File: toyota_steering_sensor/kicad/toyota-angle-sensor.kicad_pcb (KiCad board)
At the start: 2 copper layers, 32 parts, among them IC1 ATMEGA328PB-AU, IC2 LS7366R, IC3 AS5047P, J1 AVR-ISP-6, J2 RJ45, U1 NCP1117-5.0_SOT223, U2 MCP2515-xSO, U3 TJA1051T-3, Y1 16MHz, Y2 40MHz, Y3 8MHz

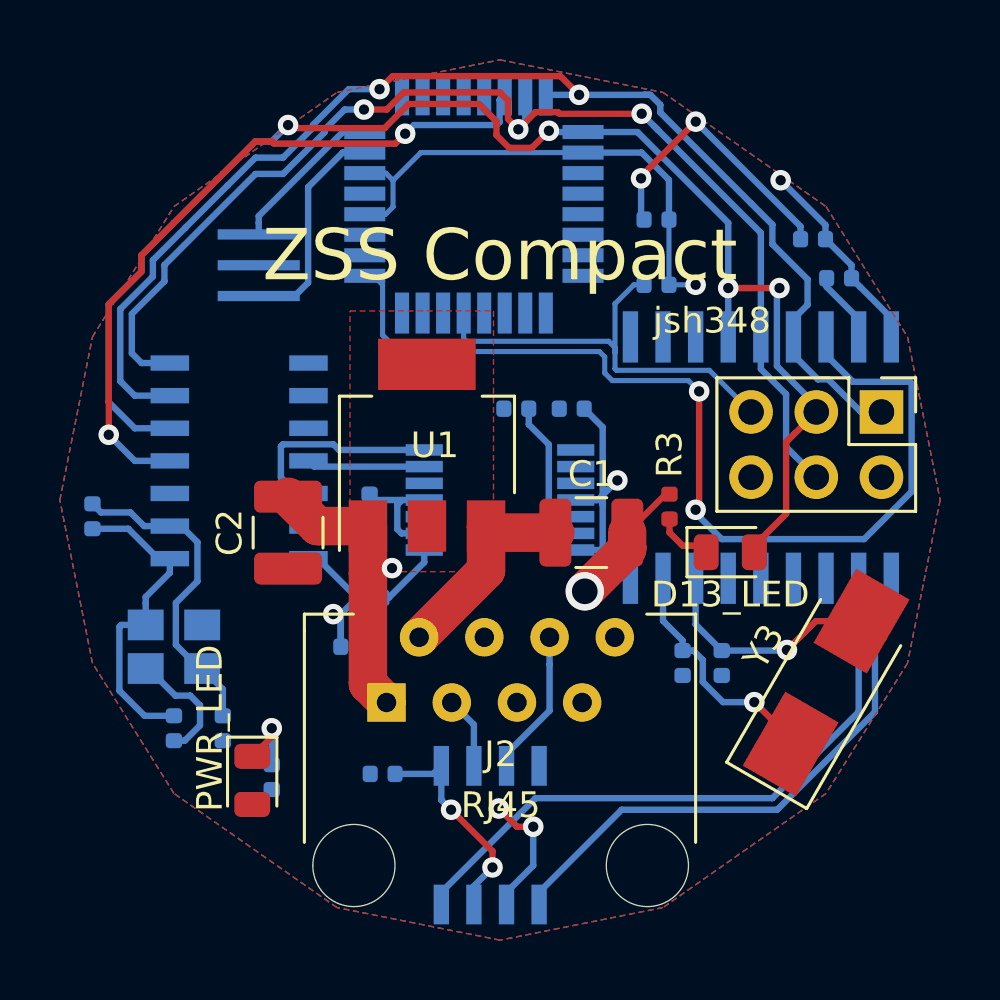
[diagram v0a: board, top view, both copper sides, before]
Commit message: moved atmega chip slightly to pass design rule check
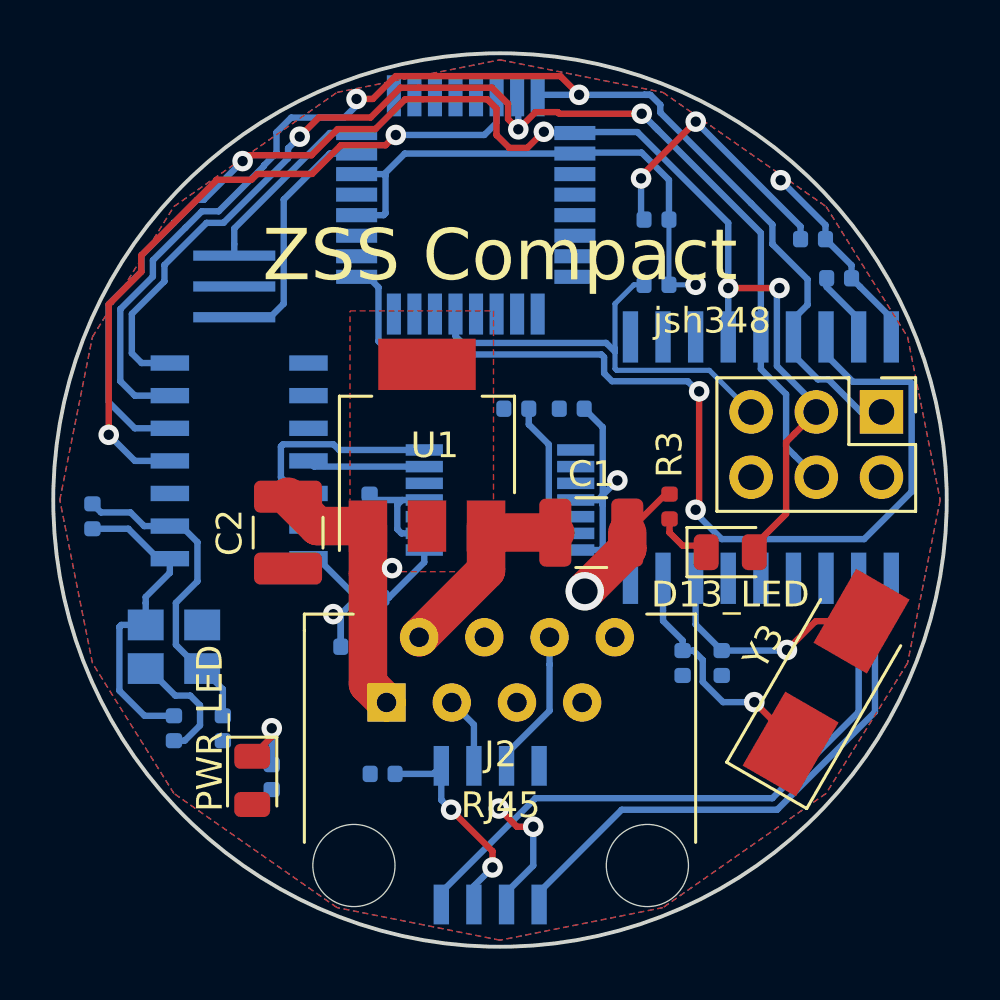
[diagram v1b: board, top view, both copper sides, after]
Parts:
- moved Y1 1.26 mm to (116.6, 118.7)
- moved IC1 0.32 mm to (125.7, 115.5)
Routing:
- net Net-(IC1-Pad7): track 8.62 -> 9.78 mm
- net Net-(IC1-Pad8): track 6.20 -> 7.36 mm
- net /D12,MISO: track 48.8 -> 49.7 mm
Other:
- board outline added: 34.8 x 34.8 mm

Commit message: modify text
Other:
- board text added: "Compact ZSS"
- board text removed: "ZSS Compact"
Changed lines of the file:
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@@
     (effects (font (size 1 1) (thickness 0.15)))
   )
-  (gr_text "ZSS Compact" (at 127 117.475) (layer F.SilkS)
+  (gr_text "Compact ZSS" (at 127 117.475) (layer F.SilkS)
     (effects (font (size 2 2) (thickness 0.15)))
   )

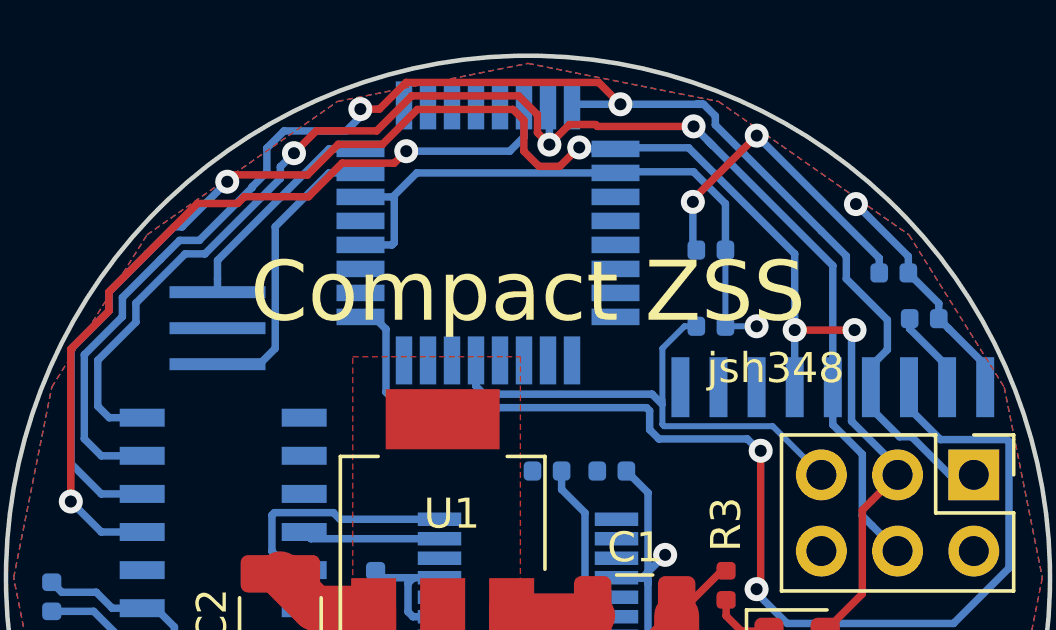
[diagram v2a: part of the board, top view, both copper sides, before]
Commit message: change texts on board
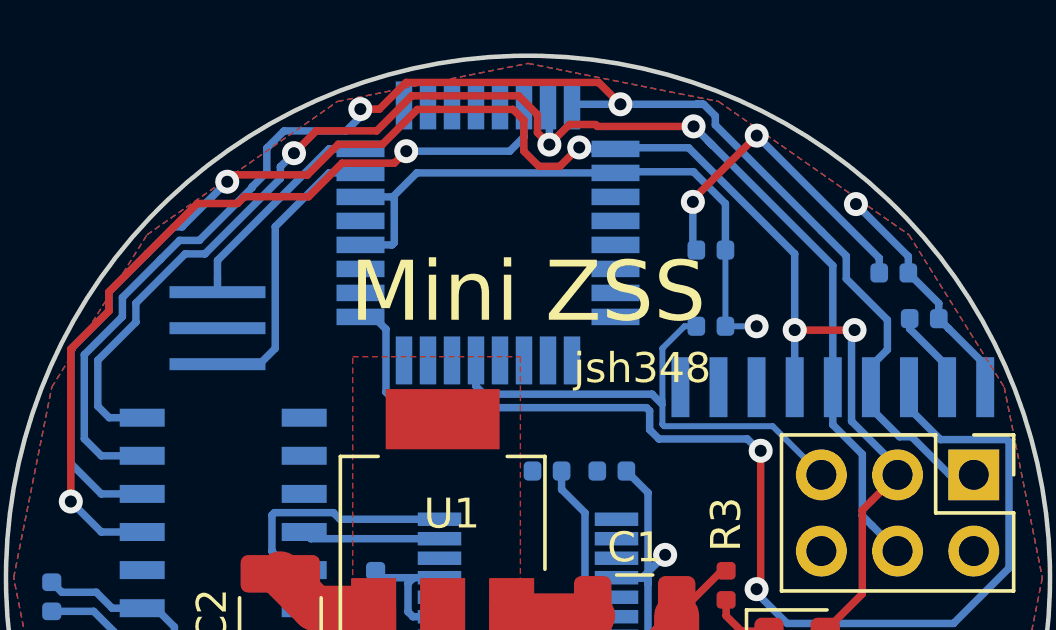
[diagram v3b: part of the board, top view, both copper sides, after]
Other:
- board text added: "Mini ZSS"
- board text removed: "Compact ZSS"
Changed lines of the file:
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@@
     (effects (font (size 1 1) (thickness 0.15)) (justify mirror))
   )
-  (gr_text jsh348 (at 135.255 120.015) (layer F.SilkS)
+  (gr_text jsh348 (at 130.81 120.015) (layer F.SilkS)
     (effects (font (size 1 1) (thickness 0.15)))
   )
-  (gr_text "Compact ZSS" (at 127 117.475) (layer F.SilkS)
+  (gr_text "Mini ZSS" (at 127 117.475) (layer F.SilkS)
     (effects (font (size 2 2) (thickness 0.15)))
   )

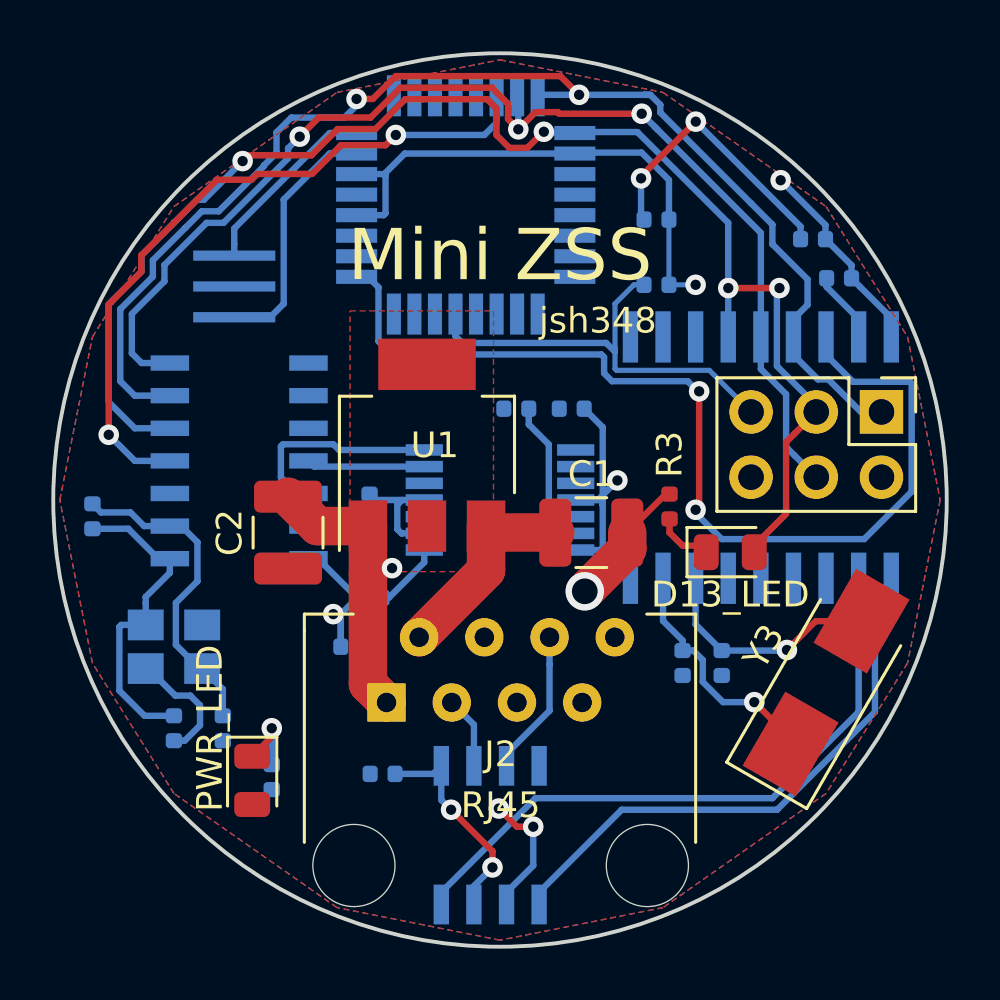
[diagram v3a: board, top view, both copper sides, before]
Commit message: change resistor and capacitor from 0402 to 0603
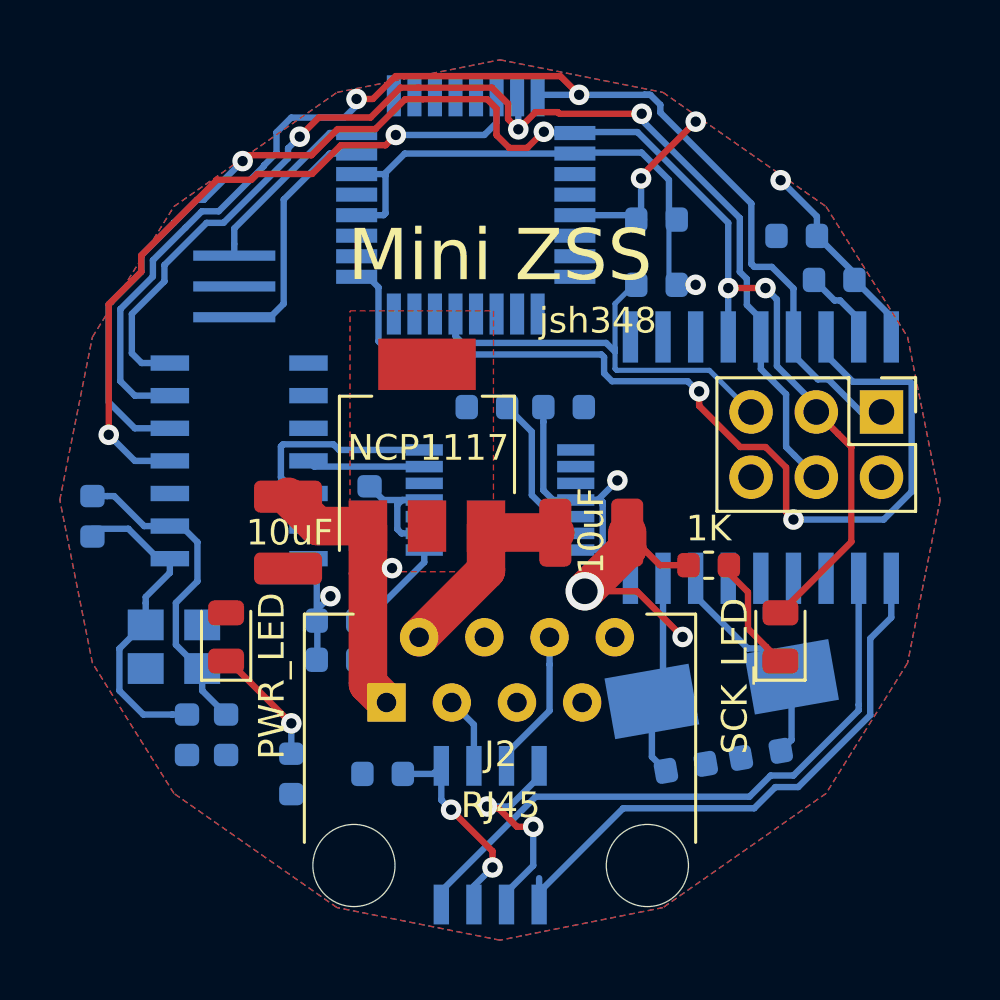
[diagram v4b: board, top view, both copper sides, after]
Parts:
- C10, C11, C12, C3, C4, C5, C6, C7, C8, C9: footprint Capacitor_SMD:C_0402_1005Metric -> Capacitor_SMD:C_0603_1608Metric
- D2: value D13_LED -> SCK_LED
- R1, R2, R3, R4, R5, R6, R7: footprint Resistor_SMD:R_0402_1005Metric -> Resistor_SMD:R_0603_1608Metric
- Y3: moved to B.Cu
- moved D1 5.68 mm to (116.3, 132.3), turned to 90 degrees
- moved Y3 4.07 mm to (135.6, 134.4), turned to 10 degrees
- moved C6 4.07 mm to (134.2, 137.4), turned to 10 degrees
- moved C5 3.87 mm to (137.2, 136.9), turned to 190 degrees
- moved D2 3.84 mm to (137.9, 132.3), turned to 90 degrees
- moved R3 2.75 mm to (135.1, 129.5), turned to 180 degrees
- moved R6 1.55 mm to (120.7, 131.7)
- moved C7 1.14 mm to (126.5, 123.4)
- moved C9 0.81 mm to (120.7, 133.2)
- moved R2 0.77 mm to (118.9, 137.7)
- moved C10 0.65 mm to (138.6, 116.7)
- moved C4 0.57 mm to (114.8, 136.1)
- moved C12 0.32 mm to (129.5, 123.4), turned to 0 degrees
- moved C3 0.28 mm to (116.3, 136.1)
- moved R5 0.20 mm to (140.0, 118.4)
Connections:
- IC1 pad 10: (no net) -> Net-(IC1-Pad10)
- IC1 pad 11: (no net) -> Net-(IC1-Pad11)
- IC1 pad 12: (no net) -> Net-(IC1-Pad12)
- IC1 pad 13: (no net) -> Net-(IC1-Pad13)
- IC1 pad 19: (no net) -> Net-(IC1-Pad19)
- IC1 pad 2: (no net) -> Net-(IC1-Pad2)
- IC1 pad 20: (no net) -> Net-(IC1-Pad20)
- IC1 pad 22: (no net) -> Net-(IC1-Pad22)
- IC1 pad 23: (no net) -> Net-(IC1-Pad23)
- IC1 pad 24: (no net) -> Net-(IC1-Pad24)
- IC1 pad 25: (no net) -> Net-(IC1-Pad25)
- IC1 pad 26: (no net) -> Net-(IC1-Pad26)
- IC1 pad 27: (no net) -> Net-(IC1-Pad27)
- IC1 pad 28: (no net) -> Net-(IC1-Pad28)
- IC1 pad 30: (no net) -> Net-(IC1-Pad30)
- IC1 pad 31: (no net) -> Net-(IC1-Pad31)
- IC1 pad 32: (no net) -> Net-(IC1-Pad32)
- IC1 pad 9: (no net) -> Net-(IC1-Pad9)
- IC2 pad 10: (no net) -> Net-(IC2-Pad10)
- IC2 pad 13: (no net) -> Net-(IC2-Pad13)
- IC2 pad 8: (no net) -> Net-(IC2-Pad8)
- IC2 pad 9: (no net) -> Net-(IC2-Pad9)
- IC3 pad 10: (no net) -> Net-(IC3-Pad10)
- IC3 pad 3: (no net) -> Net-(IC3-Pad3)
- IC3 pad 5: (no net) -> Net-(IC3-Pad5)
- IC3 pad 8: (no net) -> Net-(IC3-Pad8)
- IC3 pad 9: (no net) -> Net-(IC3-Pad9)
- J2 pad 4: (no net) -> Net-(J2-Pad4)
- J2 pad 7: (no net) -> Net-(J2-Pad7)
- J2 pad 8: (no net) -> Net-(J2-Pad8)
- U2 pad 10: (no net) -> Net-(U2-Pad10)
- U2 pad 11: (no net) -> Net-(U2-Pad11)
- U2 pad 12: (no net) -> Net-(U2-Pad12)
- U2 pad 3: (no net) -> Net-(U2-Pad3)
- U2 pad 4: (no net) -> Net-(U2-Pad4)
- U2 pad 5: (no net) -> Net-(U2-Pad5)
- U2 pad 6: (no net) -> Net-(U2-Pad6)
- Y2 pad 2: GND -> Net-(Y2-Pad2)
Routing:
- net /D13,SCK: track 55.4 -> 58.3 mm
- net Net-(D2-Pad1): track 2.17 -> 4.69 mm
- net /D3: track 39.9 -> 37.6 mm
- net Net-(D1-Pad1): track 2.83 -> 4.73 mm
- net Net-(C6-Pad1): track 9.47 -> 7.91 mm, vias 1 -> 0
- net Net-(IC3-Pad1): track 2.69 -> 3.98 mm
- net Net-(U2-Pad1): track 21.9 -> 22.9 mm
- net Net-(IC3-Pad2): track 4.56 -> 5.54 mm
- net GND: track 40.2 -> 40.5 mm, vias 6 -> 7
- net Net-(C5-Pad1): track 9.16 -> 8.79 mm, vias 1 -> 0
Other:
- board outline removed
- board text added: "NCP1117"

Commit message: modified silkscreen to show resistance and capacitance, regen gerber
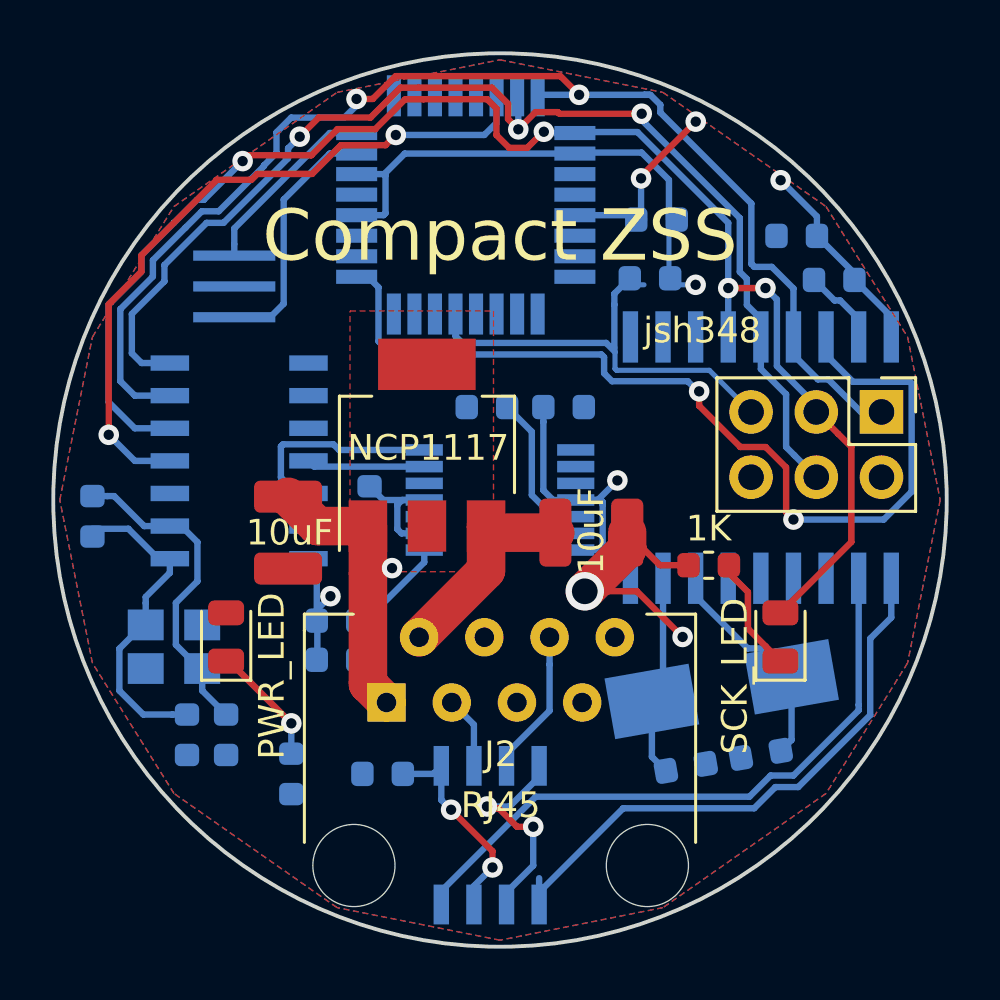
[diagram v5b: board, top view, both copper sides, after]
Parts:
- C7: value 1uF -> 1.0uF
- moved R1 0.36 mm to (132.8, 118.4)
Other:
- board outline added: 34.8 x 34.8 mm
- board text added: "16MHz"
- board text added: "Compact ZSS"
- board text removed: "Mini ZSS"

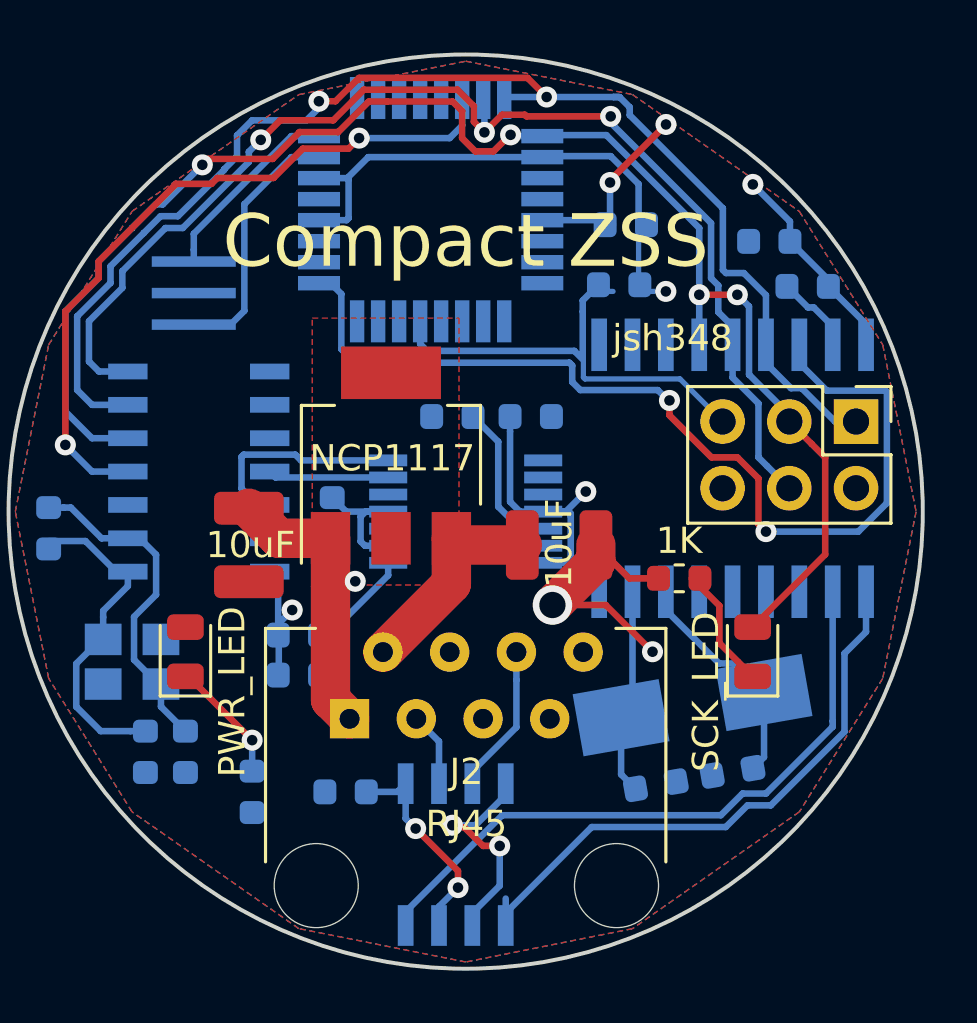
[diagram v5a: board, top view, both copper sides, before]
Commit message: modify silkscreen text for angle sensor, added graphics, regen gerber
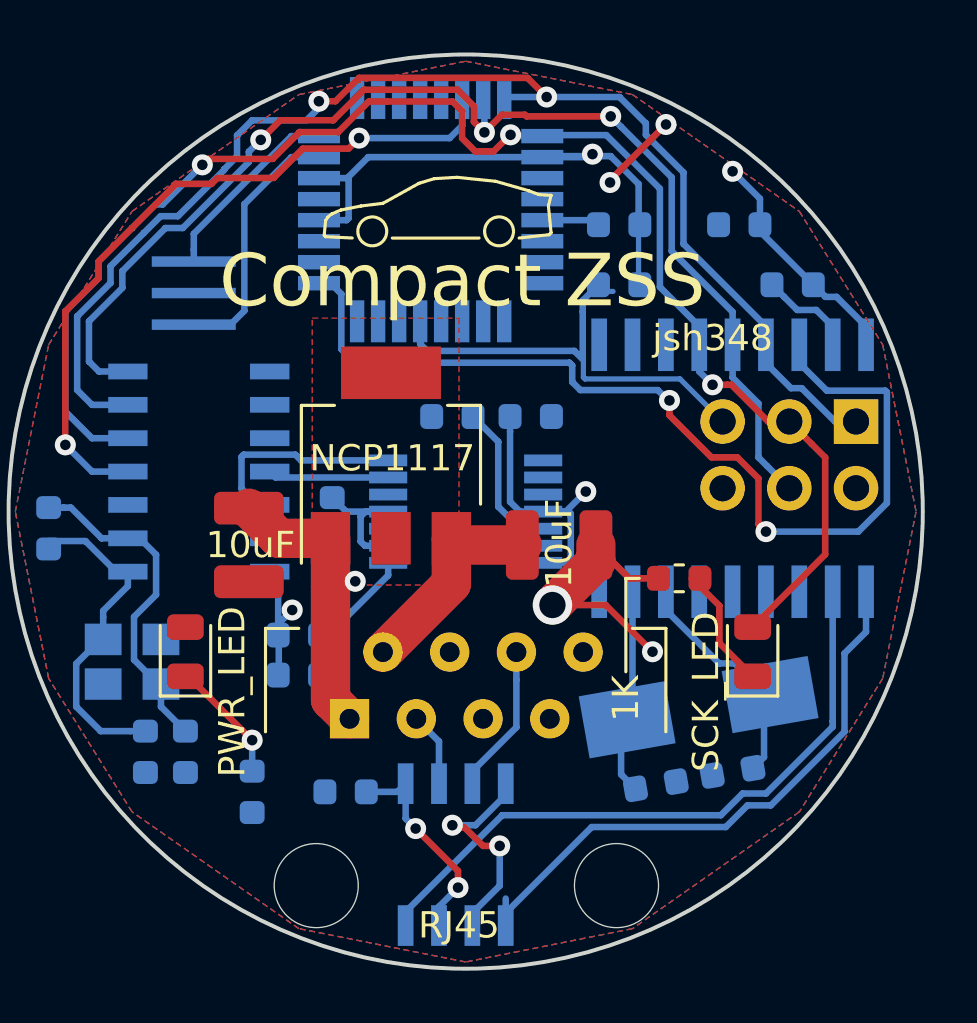
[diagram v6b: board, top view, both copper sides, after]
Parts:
- U2: value MCP2515-xSO -> MCP2515
- U3: value TJA1051T-3 -> TJA1050
- moved C10 1.31 mm to (137.4, 116.1)
- moved R5 0.58 mm to (139.4, 118.4)
- moved C8 0.25 mm to (132.8, 116.1)
- moved Y3 0.24 mm to (135.9, 134.4)
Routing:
- net +5V: track 52.5 -> 54.5 mm
- net /D13,SCK: track 58.3 -> 56.5 mm, vias 4 -> 3
- net GND: track 40.5 -> 38.9 mm
- net Net-(R5-Pad2): track 3.07 -> 3.67 mm
- net /D12,MISO: track 49.7 -> 49.1 mm
